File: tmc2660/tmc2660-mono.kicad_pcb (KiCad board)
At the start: 4 copper layers, 25 x 40 mm, 19 parts, among them J1 0R, P3 Motor, U1 TMC2660

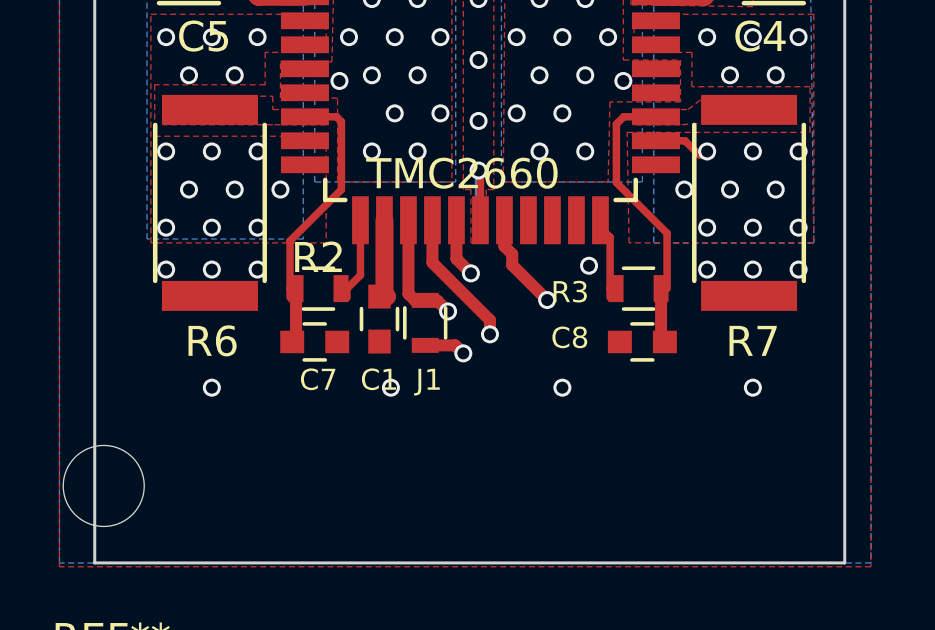
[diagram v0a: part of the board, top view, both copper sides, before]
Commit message: Add ~ENABLE to the bus.
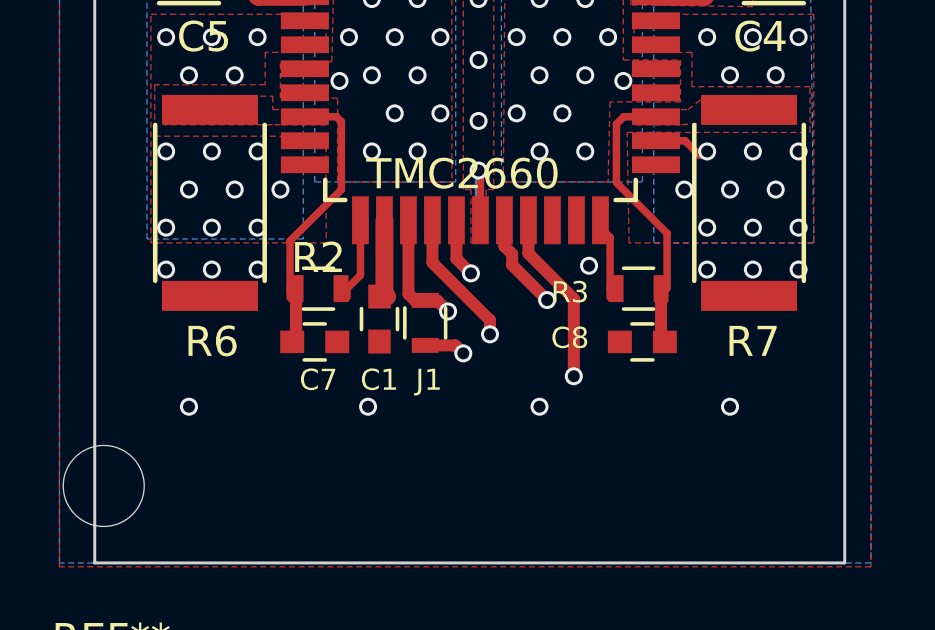
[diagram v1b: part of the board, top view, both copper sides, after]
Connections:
- U1 pad 19: GND -> ~ENABLE
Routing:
- net ~ENABLE: track 0.00 -> 33.4 mm, vias 0 -> 1
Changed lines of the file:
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@@
     (thickness 1.6)
     (drawings 7)
-    (tracks 198)
+    (tracks 205)
     (zones 0)
     (modules 19)
-    (nets 23)
+    (nets 24)
   )
   (page A4)
@@
   )
   (setup
-    (last_trace_width 0.25)
+    (last_trace_width 0.4)
     (user_trace_width 0.4)
     (user_trace_width 0.6)
@@
   (net 21 "Net-(R3-Pad2)")
   (net 22 GLOBAL_MISO)
+  (net 23 ~ENABLE)
   (net_class Default "This is the default net class."
     (clearance 0.127)
@@
     (add_net "Net-(U1-Pad43)")
     (add_net VCC)
+    (add_net ~ENABLE)
   )
   (net_class MotPower ""
@@
       (net 19 /CS_1))
     (pad 19 smd rect (at 1.6 5.85 90) (size 1.6 0.56) (layers F.Cu F.Paste F.Mask)
-      (net 1 GND))
+      (net 23 ~ENABLE))
     (pad 20 smd rect (at 2.4 5.85 90) (size 1.6 0.56) (layers F.Cu F.Paste F.Mask))
     (pad 21 smd rect (at 3.2 5.85 90) (size 1.6 0.56) (layers F.Cu F.Paste F.Mask)
@@
   (gr_line (start 117 31.623) (end 142 31.623) (layer Edge.Cuts) (width 0.1))
   (via (at 133.477 61.722) (size 0.6) (drill 0.4) (layers F.Cu B.Cu) (net 1))
-  (via (at 138.938 65.786) (size 0.6) (drill 0.4) (layers F.Cu B.Cu) (net 1))
-  (via (at 132.588 65.786) (size 0.6) (drill 0.4) (layers F.Cu B.Cu) (net 1))
-  (via (at 126.873 65.786) (size 0.6) (drill 0.4) (layers F.Cu B.Cu) (net 1))
-  (via (at 120.904 65.786) (size 0.6) (drill 0.4) (layers F.Cu B.Cu) (net 1))
+  (via (at 138.176 66.421) (size 0.6) (drill 0.4) (layers F.Cu B.Cu) (net 1))
+  (via (at 131.826 66.421) (size 0.6) (drill 0.4) (layers F.Cu B.Cu) (net 1))
+  (via (at 126.111 66.421) (size 0.6) (drill 0.4) (layers F.Cu B.Cu) (net 1))
+  (via (at 120.142 66.421) (size 0.6) (drill 0.4) (layers F.Cu B.Cu) (net 1))
   (segment (start 129.8575 48.506) (end 129.8575 47.1685) (width 0.6) (layer F.Cu) (net 1))
   (segment (start 129.8575 47.1685) (end 130.544 46.482) (width 0.6) (layer F.Cu) (net 1))
@@
   (segment (start 134.178 60.772) (end 134.178 62.484) (width 0.25) (layer F.Cu) (net 21) (status 20))
   (segment (start 133.8575 60.206) (end 133.8575 60.4515) (width 0.25) (layer F.Cu) (net 21) (status 30))
+  (segment (start 131.4575 60.206) (end 131.4575 61.314538) (width 0.4) (layer F.Cu) (net 23))
+  (segment (start 131.4575 61.314538) (end 132.969 62.826038) (width 0.4) (layer F.Cu) (net 23))
+  (segment (start 132.969 62.826038) (end 132.969 64.980736) (width 0.4) (layer F.Cu) (net 23))
+  (segment (start 132.969 64.980736) (end 132.969 65.405) (width 0.4) (layer F.Cu) (net 23))
+  (segment (start 132.969 65.405) (end 143.256 65.405) (width 0.4) (layer In1.Cu) (net 23))
+  (segment (start 132.969 65.405) (end 115.697 65.405) (width 0.4) (layer In1.Cu) (net 23))
+  (via (at 132.969 65.405) (size 0.6) (drill 0.4) (layers F.Cu B.Cu) (net 23))
   (segment (start 128.397 64.377) (end 129.02 64.377) (width 0.4) (layer F.Cu) (net 22))
   (segment (start 129.02 64.377) (end 129.286 64.643) (width 0.4) (layer F.Cu) (net 22))
@@
     (min_thickness 0.254)
     (keepout (tracks not_allowed) (vias not_allowed) (copperpour not_allowed))
-    (fill (arc_segments 16) (thermal_gap 0.508) (thermal_bridge_width 0.508))
-    (polygon
-      (pts
+    (fill yes (arc_segments 16) (thermal_gap 0.508) (thermal_bridge_width 0.508))
+    (polygon
+      (pts

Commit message: First transition into hierachical sheets.
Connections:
- net /BRA renamed /TMC2660-Block/BRA
- net /BRB renamed /TMC2660-Block/BRB
- net /CS_1 renamed /TMC2660-Block/CS
- net /DIR_1 renamed /TMC2660-Block/DIR
- net /MISO_1 renamed /TMC2660-Block/MISO
- net /MOSI_1 renamed /TMC2660-Block/MOSI
- net /SCLK_1 renamed /TMC2660-Block/SCLK
- net /STEP_1 renamed /TMC2660-Block/STEP
- net 1A1 renamed /TMC2660-Block/A1
- net 1A2 renamed /TMC2660-Block/A2
- net 1B1 renamed /TMC2660-Block/B1
- net 1B2 renamed /TMC2660-Block/B2
- net GLOBAL_MISO renamed /TMC2660-Block/GLOBAL_MISO
- net ~ENABLE renamed /TMC2660-Block/~EN

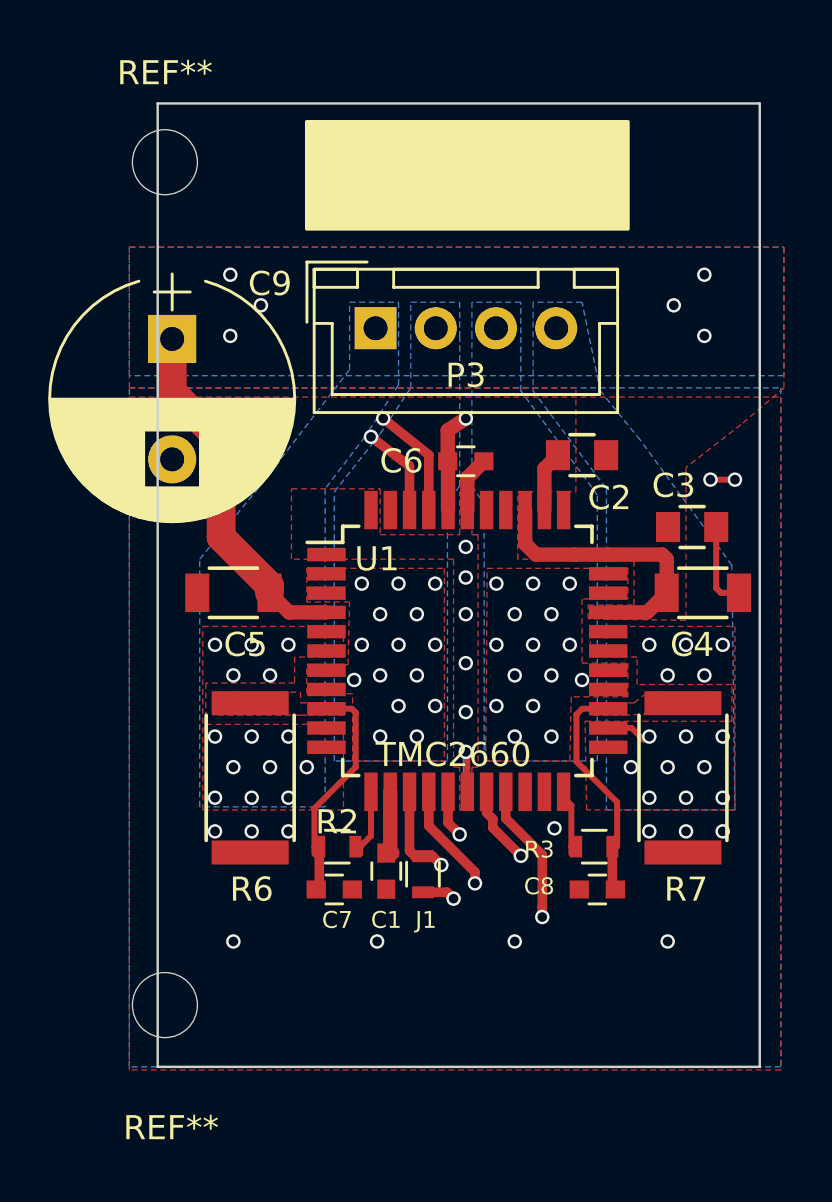
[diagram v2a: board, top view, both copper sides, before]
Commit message: More sensible annotations, starting in the 100 range.
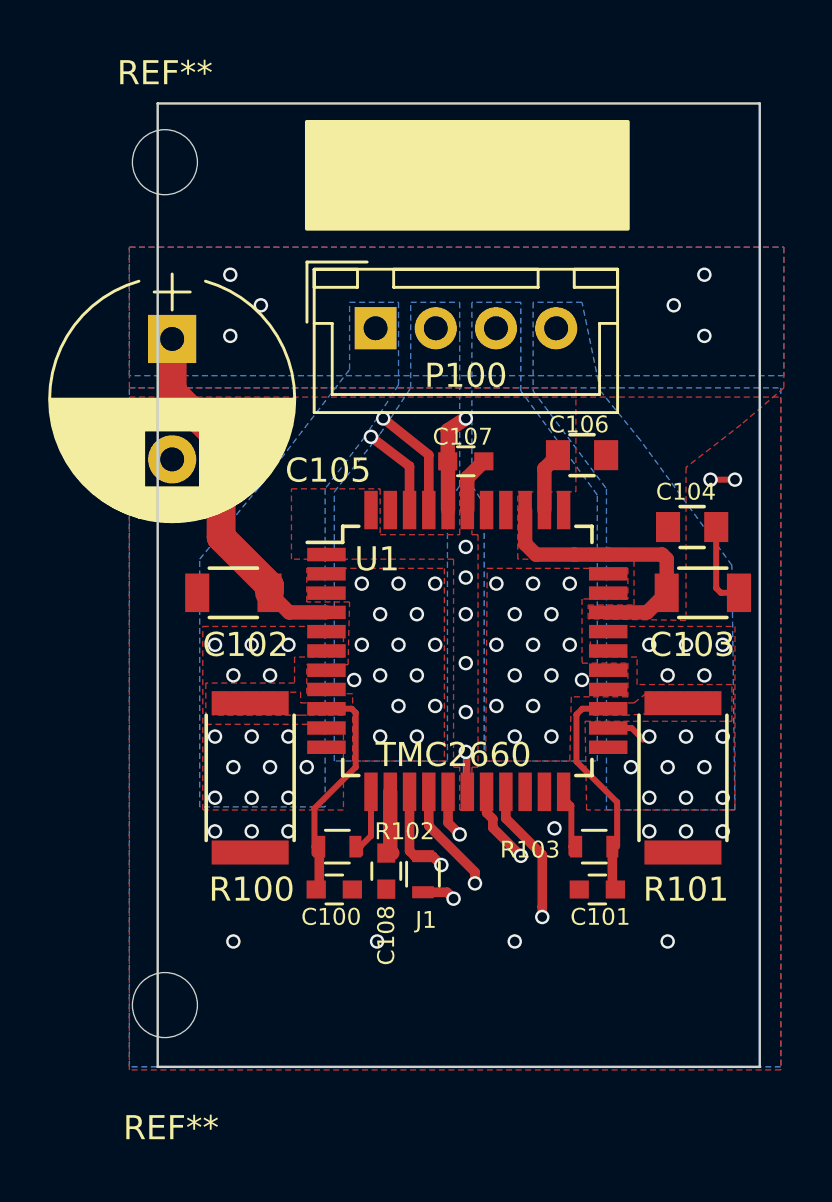
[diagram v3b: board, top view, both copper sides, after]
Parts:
- removed C4: 10u, Capacitors_SMD:C_1206
- added C103: 10u, Capacitors_SMD:C_1206, F.Cu at (139.6, 51.9)
- renumbered C7 to C100, C8 to C101, C5 to C102, C3 to C104, C9 to C105, C2 to C106, C6 to C107, C1 to C108, P3 to P100, R6 to R100, R7 to R101, R2 to R102, R3 to R103

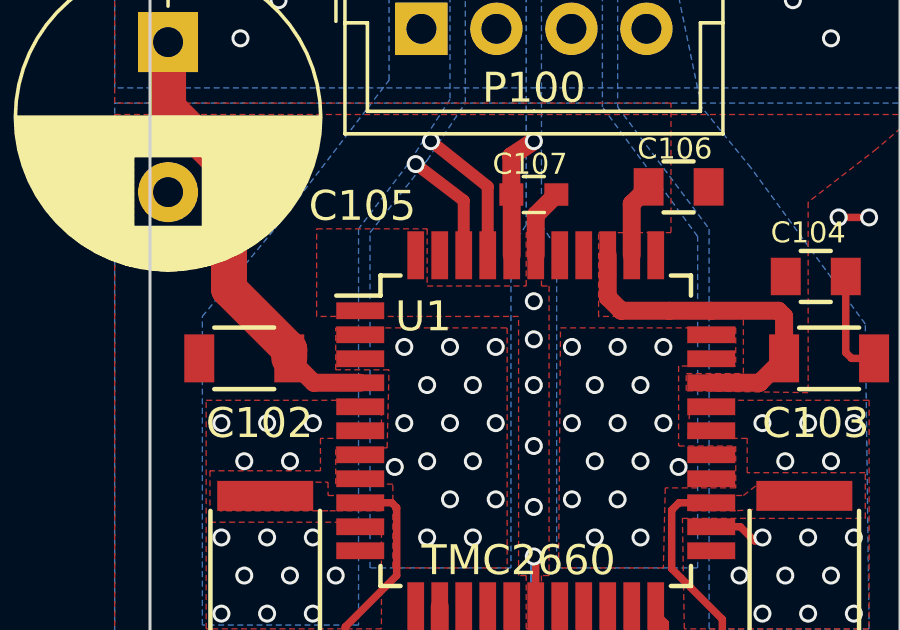
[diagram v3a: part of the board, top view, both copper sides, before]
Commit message: Numbering scheme: have U1 be U100.
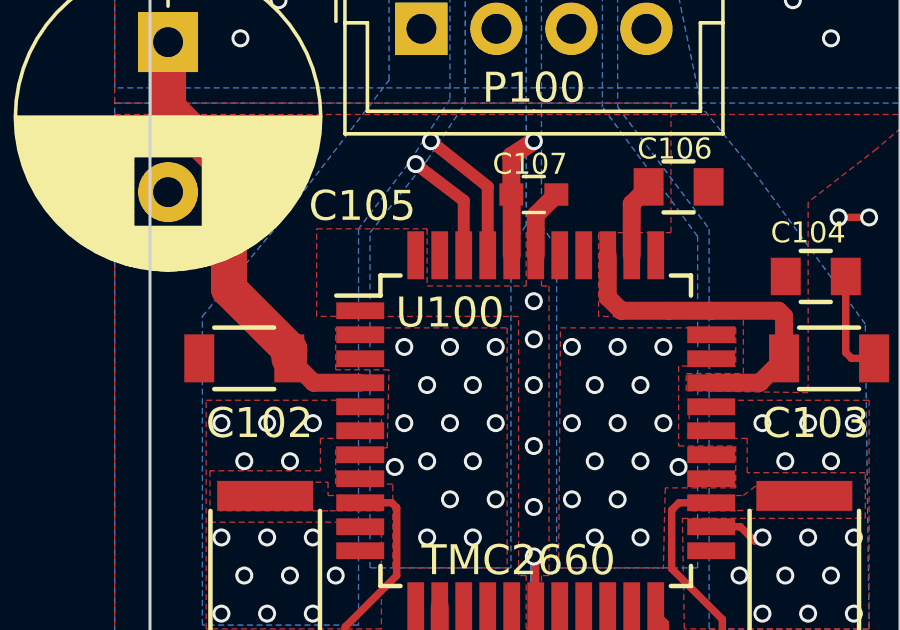
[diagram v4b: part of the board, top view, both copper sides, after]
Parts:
- renumbered U1 to U100

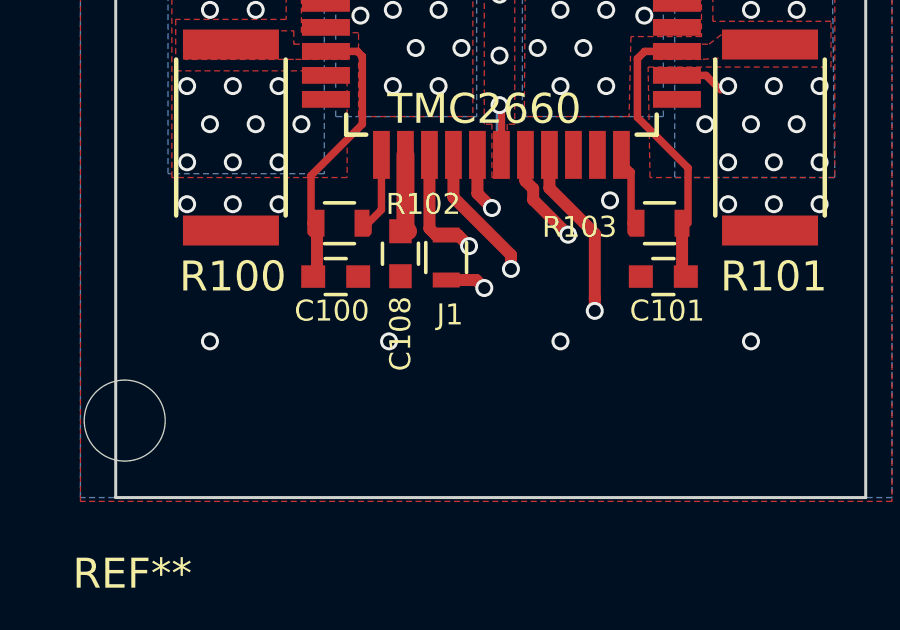
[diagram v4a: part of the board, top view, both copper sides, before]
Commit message: J1 -> J100
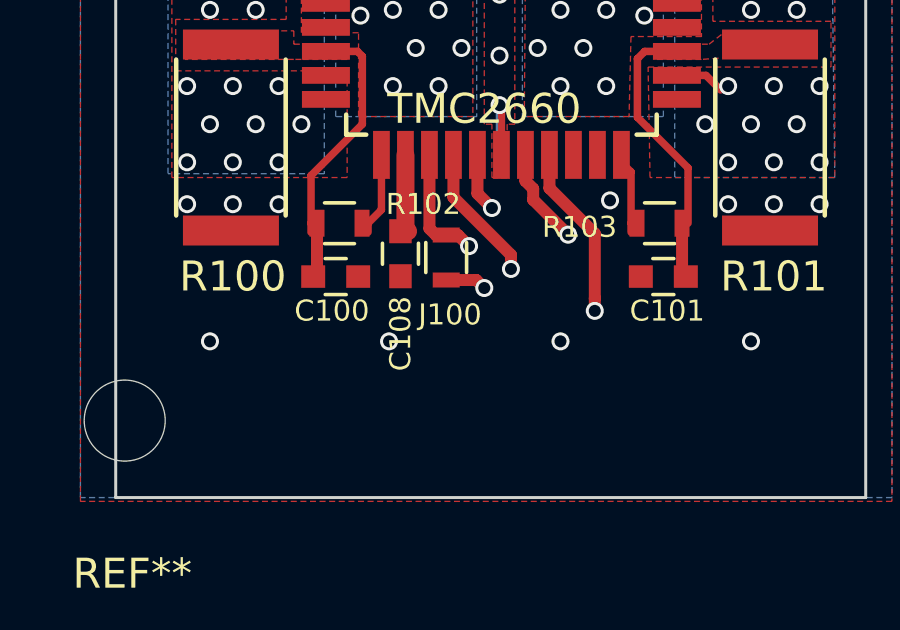
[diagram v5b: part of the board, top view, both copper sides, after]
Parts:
- renumbered J1 to J100
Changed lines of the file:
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@@
     (tags "resistor 0603")
     (attr smd)
-    (fp_text reference J1 (at -1.905 0.127) (layer F.SilkS)
+    (fp_text reference J100 (at -1.905 0.127) (layer F.SilkS)
       (effects (font (size 0.7 0.7) (thickness 0.12)))
     )
